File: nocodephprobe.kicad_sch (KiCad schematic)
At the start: 31 parts, among them J1 RF1-01 BNC, J2 10K, Q1 2N7002, U1 LMV358a, U2 ICL7106CPL, U3 MCP1501-10xCH, U4 VI-302-DP-RC-S

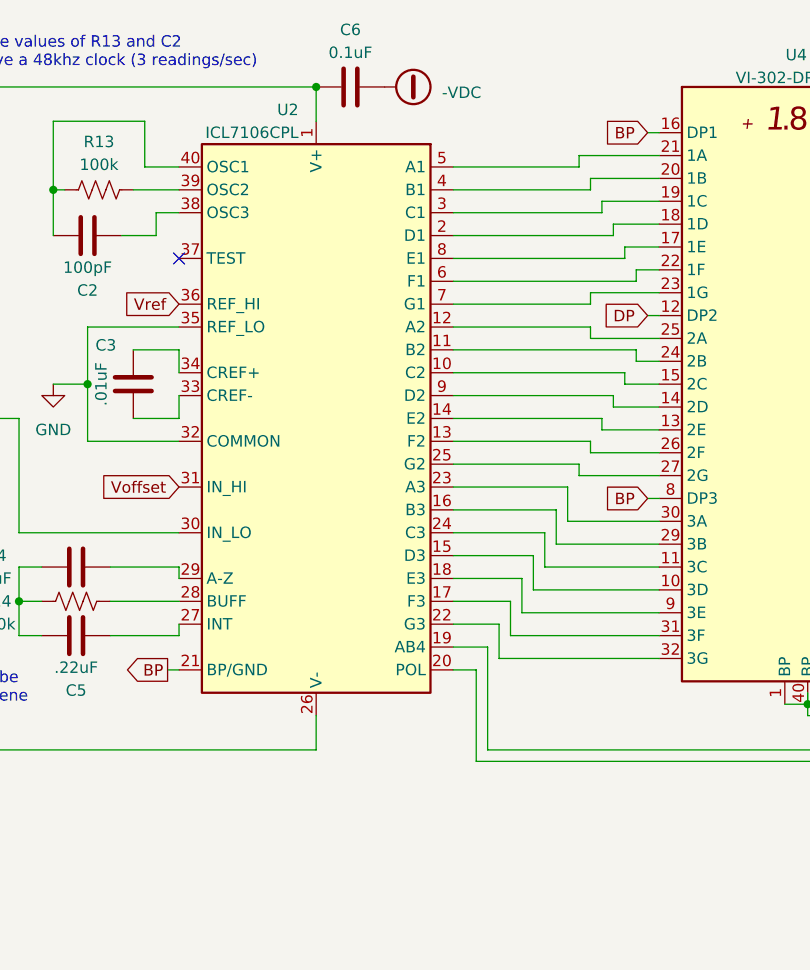
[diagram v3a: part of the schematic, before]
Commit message: Initial routing of nets
No DRC errors, but some mess vias and traces.
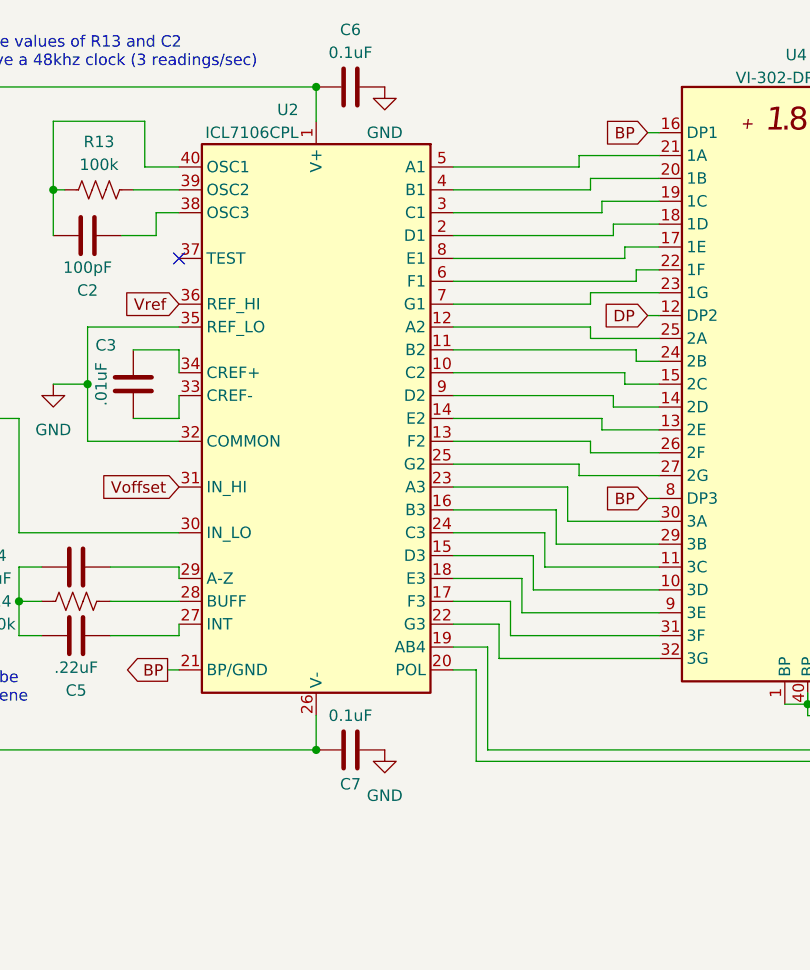
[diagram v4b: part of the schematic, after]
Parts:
- added C7: 0.1uF, Capacitor_SMD:C_0805_2012Metric_Pad1.18x1.45mm_HandSolder, symbol Device:C
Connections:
- net -VDC: now also C7.1; no longer C6.2
- net GND: now also C6.2, C7.2
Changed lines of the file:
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@@
   (junction (at 27.94 63.5) (diameter 0) (color 0 0 0 0)
+  )
+  (junction (at 203.2 100.33) (diameter 0) (color 0 0 0 0)
   )
   (junction (at 72.39 100.33) (diameter 0) (color 0 0 0 0)
@@
         (path "/2036f74b-8ede-4e4d-84df-8cc119de9ab1"
           (reference "R14") (unit 1)
+        )
+      )
+    )
+  )
+  (symbol (lib_id "Device:C") (at 207.01 100.33 90) (unit 1)
+    (in_bom yes) (on_board yes) (dnp no)
+    (property "Reference" "C7" (at 207.01 104.14 90)
+      (effects (font (size 1.27 1.27)))
+    )
+    (property "Value" "0.1uF" (at 207.01 96.52 90)
+      (effects (font (size 1.27 1.27)))
+    )
+    (property "Footprint" "Capacitor_SMD:C_0805_2012Metric_Pad1.18x1.45mm_HandSolder" (at 210.82 99.3648 0)
+      (effects (font (size 1.27 1.27)) hide)
+    )
+    (property "Datasheet" "~" (at 207.01 100.33 0)
+      (effects (font (size 1.27 1.27)) hide)
+    )
+    (pin "1")
+    (pin "2")
+    (instances
+      (project "nocodephprobe"
+        (path "/2036f74b-8ede-4e4d-84df-8cc119de9ab1"
+          (reference "C7") (unit 1)
         )
       )
@@
     )
   )
-  (symbol (lib_id "power:-VDC") (at 210.82 26.67 270) (unit 1)
-    (in_bom yes) (on_board yes) (dnp no) (fields_autoplaced)
-    (property "Reference" "#PWR011" (at 208.28 26.67 0)
-      (effects (font (size 1.27 1.27)) hide)
-    )
-    (property "Value" "-VDC" (at 217.17 27.305 90)
-      (effects (font (size 1.27 1.27)) (justify left))
-    )
-    (property "Footprint" "" (at 210.82 26.67 0)
-      (effects (font (size 1.27 1.27)) hide)
-    )
-    (property "Datasheet" "" (at 210.82 26.67 0)
-      (effects (font (size 1.27 1.27)) hide)
-    )
-    (pin "1")
-    (instances
-      (project "nocodephprobe"
-        (path "/2036f74b-8ede-4e4d-84df-8cc119de9ab1"
-          (reference "#PWR011") (unit 1)
-        )
-      )
-    )
-  )
   (symbol (lib_id "Device:R_US") (at 132.08 86.36 270) (unit 1)
     (in_bom yes) (on_board yes) (dnp no) (fields_autoplaced)
@@
         (path "/2036f74b-8ede-4e4d-84df-8cc119de9ab1"
           (reference "#PWR09") (unit 1)
+        )
+      )
+    )
+  )
+  (symbol (lib_id "power:GND") (at 210.82 100.33 0) (unit 1)
+    (in_bom yes) (on_board yes) (dnp no) (fields_autoplaced)
+    (property "Reference" "#PWR011" (at 210.82 106.68 0)
+      (effects (font (size 1.27 1.27)) hide)
+    )
+    (property "Value" "GND" (at 210.82 105.41 0)
+      (effects (font (size 1.27 1.27)))
+    )
+    (property "Footprint" "" (at 210.82 100.33 0)
+      (effects (font (size 1.27 1.27)) hide)
+    )
+    (property "Datasheet" "" (at 210.82 100.33 0)
+      (effects (font (size 1.27 1.27)) hide)
+    )
+    (pin "1")
+    (instances
+      (project "nocodephprobe"
+        (path "/2036f74b-8ede-4e4d-84df-8cc119de9ab1"
+          (reference "#PWR011") (unit 1)
         )
       )
@@
         )
       )
+    )
+  )
+  (symbol (lib_id "power:GND") (at 210.82 26.67 0) (unit 1)
+    (in_bom yes) (on_board yes) (dnp no) (fields_autoplaced)
+    (property "Reference" "#PWR010" (at 210.82 33.02 0)
+      (effects (font (size 1.27 1.27)) hide)
+    )
+    (property "Value" "GND" (at 210.82 31.75 0)
+      (effects (font (size 1.27 1.27)))
+    )
+    (property "Footprint" "" (at 210.82 26.67 0)
+      (effects (font (size 1.27 1.27)) hide)
+    )
+    (property "Datasheet" "" (at 210.82 26.67 0)
+      (effects (font (size 1.27 1.27)) hide)
+    )
+    (pin "1")
+    (instances
+      (project "nocodephprobe"
+        (path "/2036f74b-8ede-4e4d-84df-8cc119de9ab1"
+          (reference "#PWR010") (unit 1)
+        )
+      )

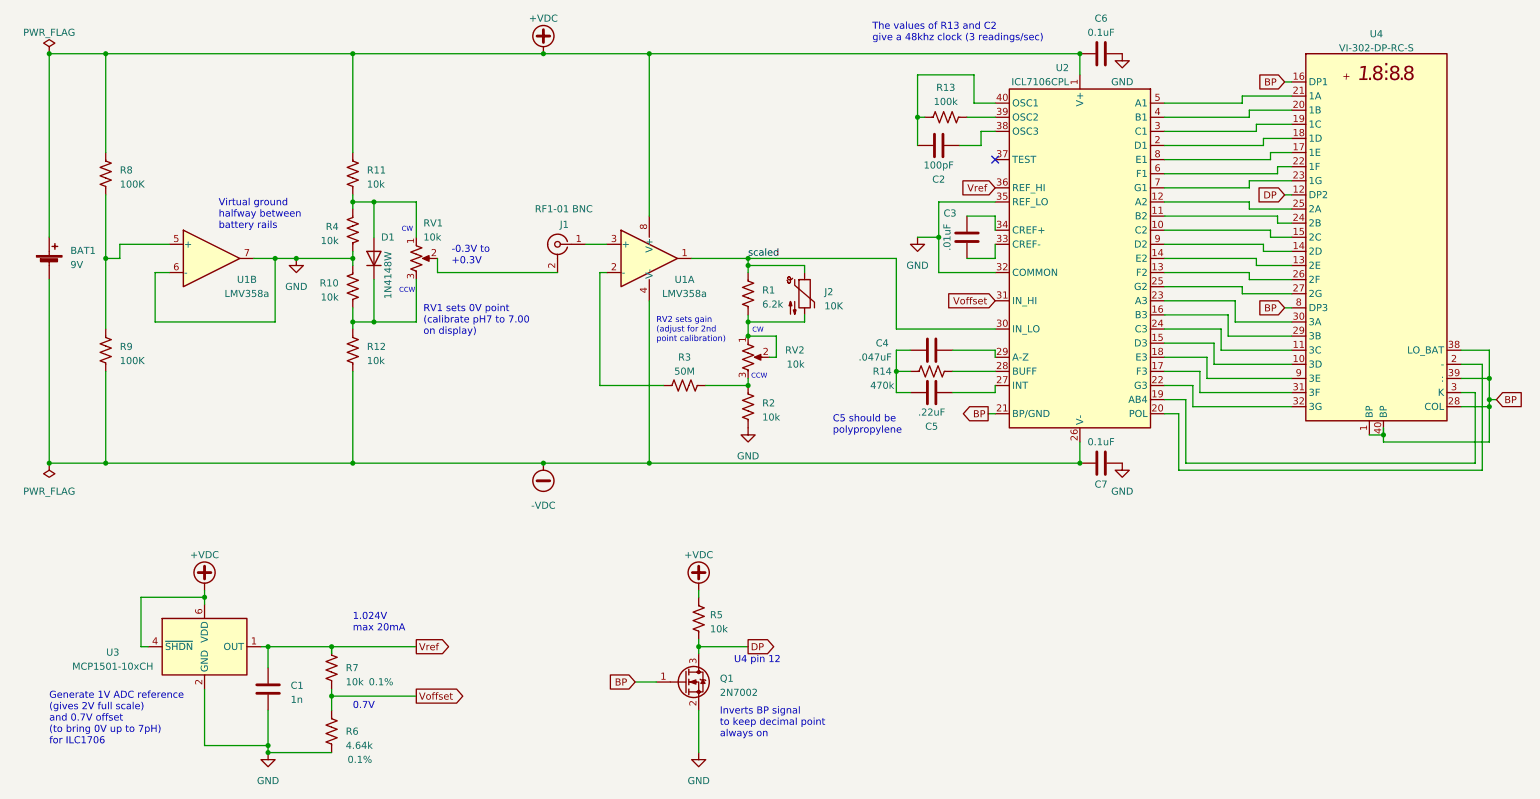
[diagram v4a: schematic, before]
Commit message: Remove redundant voltage divider
This removes two resistors.
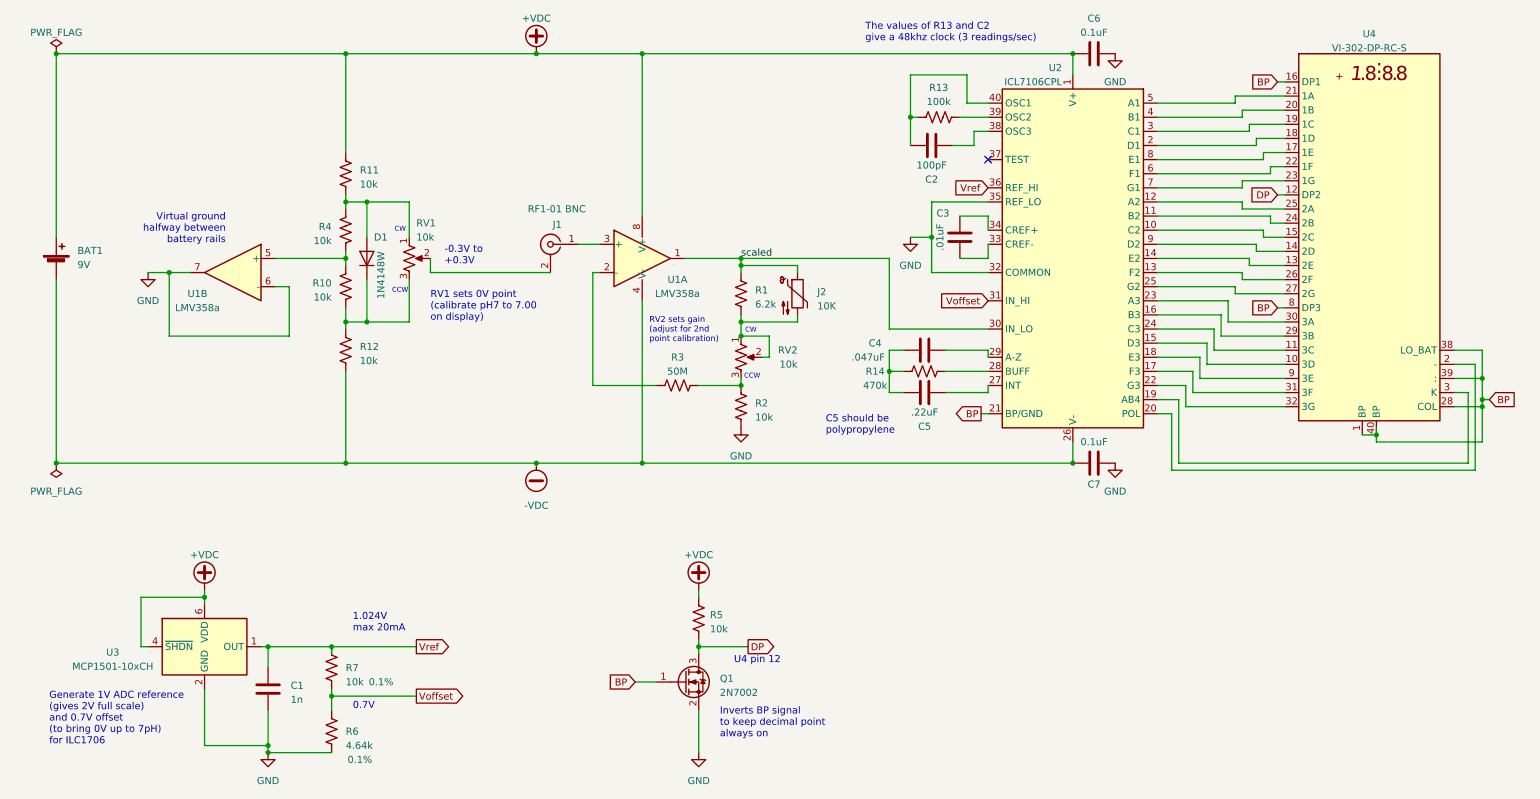
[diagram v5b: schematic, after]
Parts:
- removed R8, R9: 100K, Resistor_SMD:R_0805_2012Metric_Pad1.20x1.40mm_HandSolder, symbol Device:R_US
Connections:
- net GND: no longer R10.2, R4.1
- net at U1.5 (+): now also R10.2, R4.1
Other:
- moved on the sheet: BAT1, C2, C3, C4, C5, C6, C7, D1, J1, J2, R1, R10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

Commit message: Correct Cref (C3 value)
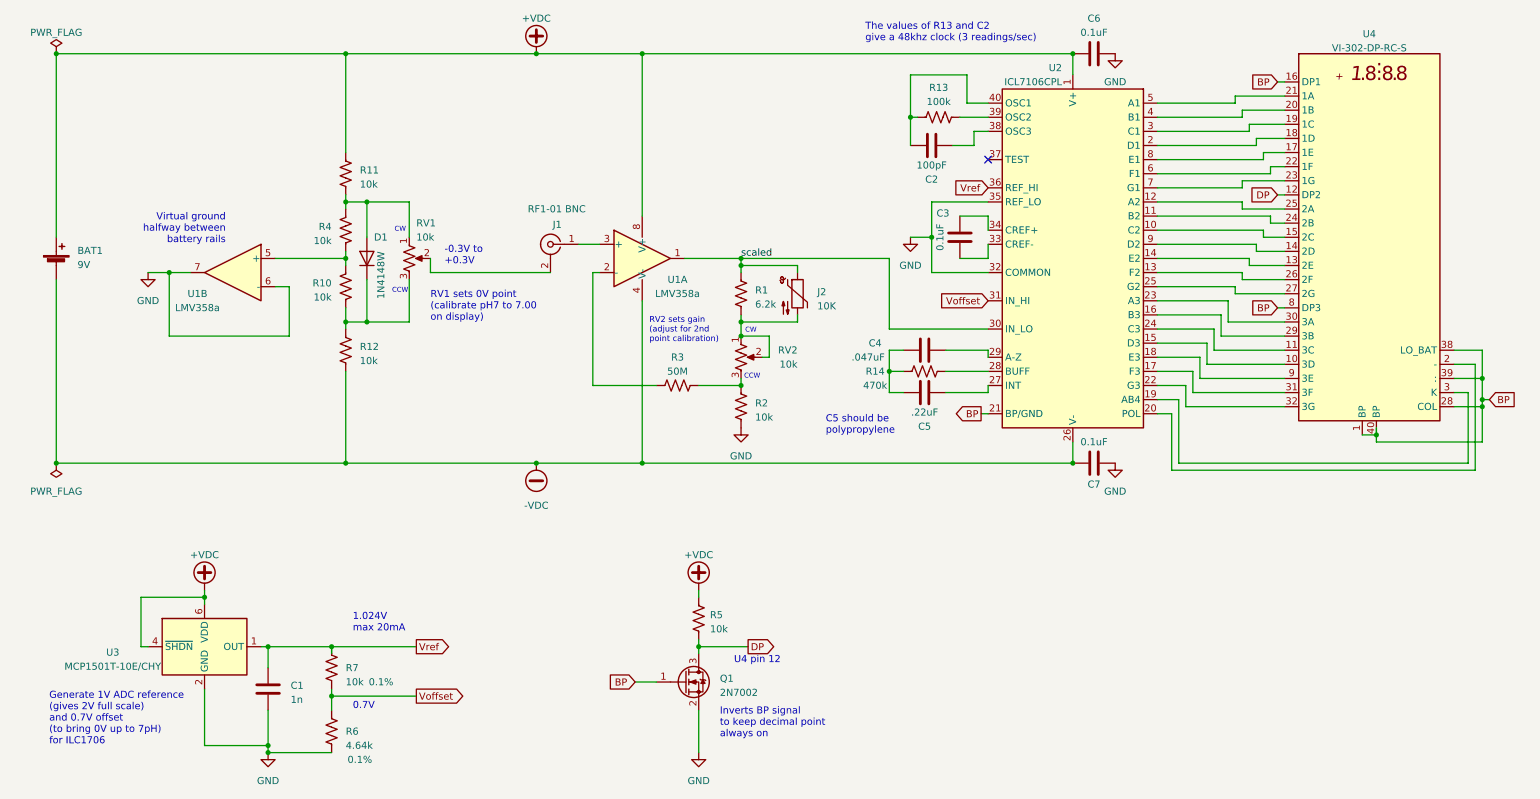
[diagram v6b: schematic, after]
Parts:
- C3: value .01uF -> 0.1uF
- U3: value MCP1501-10xCH -> MCP1501T-10E/CHY
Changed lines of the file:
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@@
       (effects (font (size 1.27 1.27)))
     )
-    (property "Value" ".01uF" (at 178.054 59.69 90)
+    (property "Value" "0.1uF" (at 178.054 59.69 90)
       (effects (font (size 1.27 1.27)))
     )
@@
       (effects (font (size 1.27 1.27)))
     )
-    (property "Value" "MCP1501-10xCH" (at 29.21 136.906 0)
-      (effects (font (size 1.27 1.27)))
-    )
+    (property "Value" "MCP1501T-10E/CHY" (at 29.21 136.906 0)
+      (effects (font (size 1.27 1.27)))
+    )
